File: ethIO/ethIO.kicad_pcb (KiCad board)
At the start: 4 copper layers, 30 x 50 mm, 62 parts, among them IC3 TLV61225DC, J6 MISC, J7 HR911130A1, U10 RTL8211E-VB-CG, Y1 25MHz

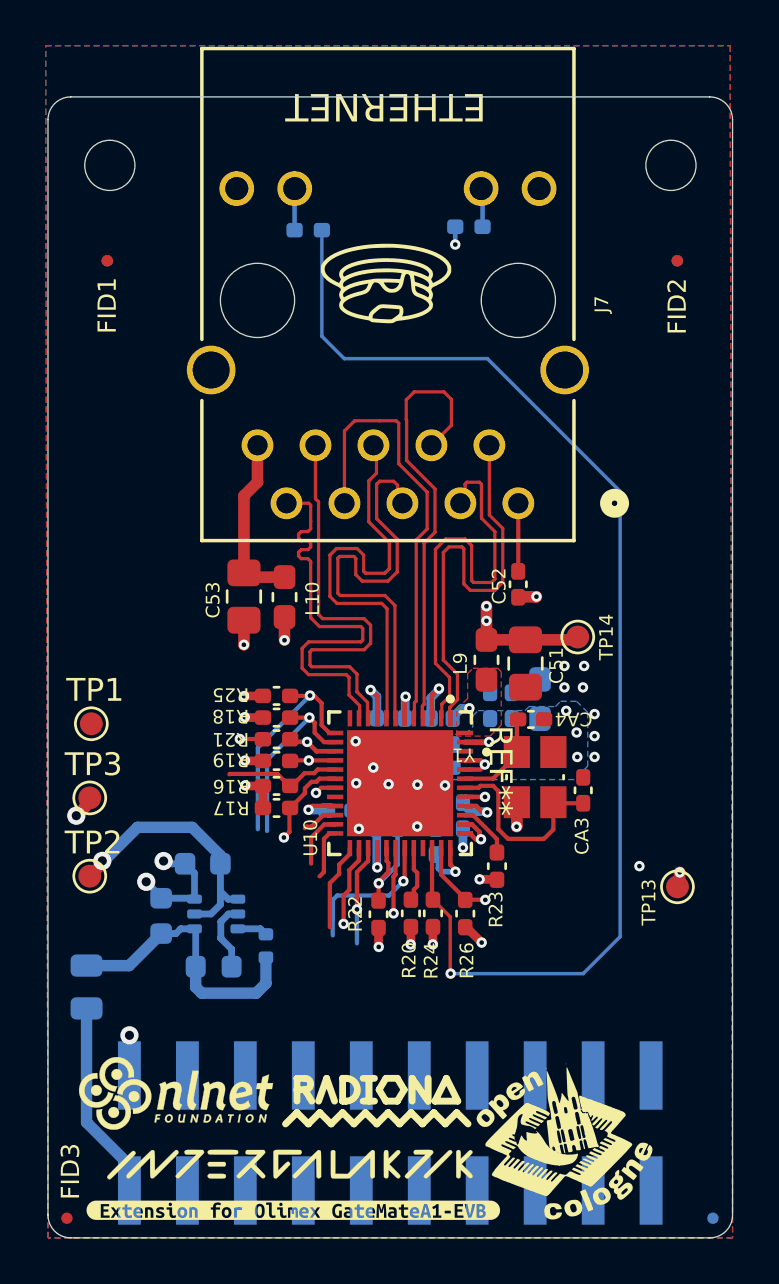
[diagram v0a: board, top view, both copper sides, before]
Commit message: Updating ethIO
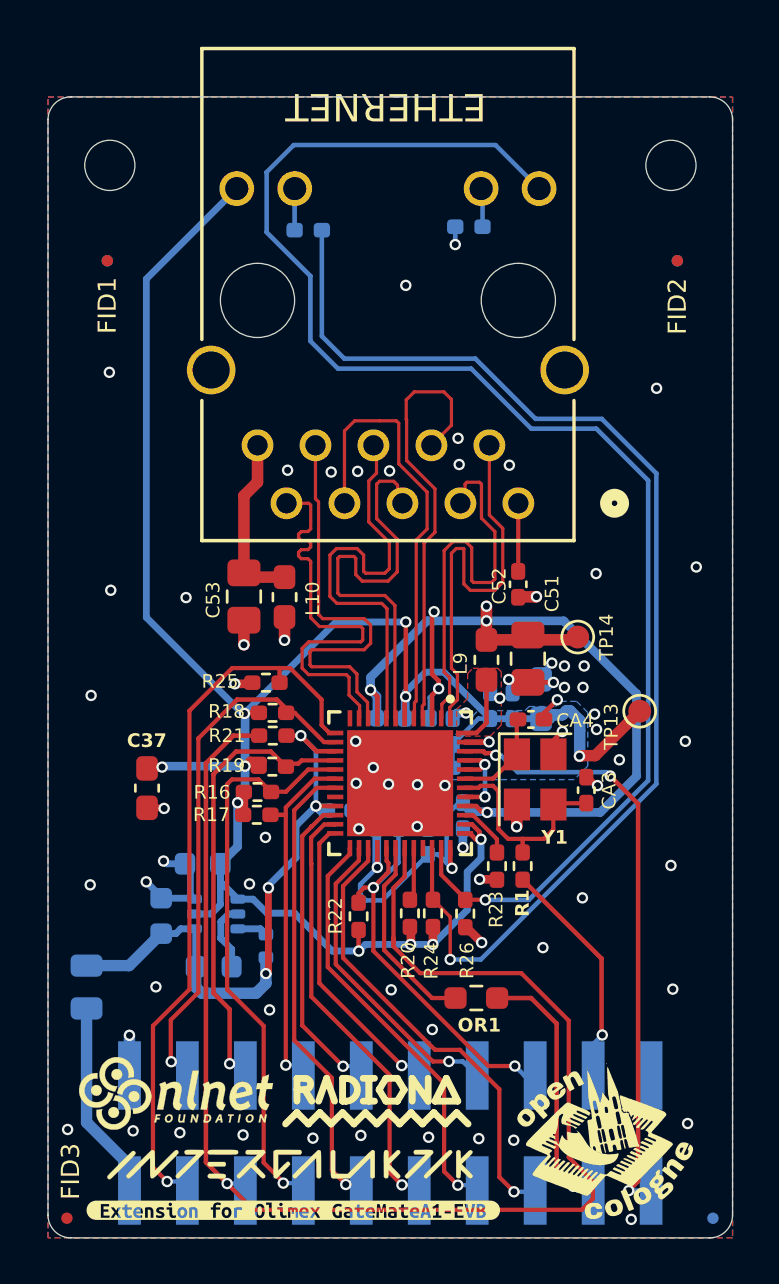
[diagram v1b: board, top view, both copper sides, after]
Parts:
- removed G***: LOGO, memes:pancakes
- removed TP1: 3V3, TestPoint:TestPoint_Pad_D1.0mm
- removed TP2: 2V5, TestPoint:TestPoint_Pad_D1.0mm
- removed TP3: GND, TestPoint:TestPoint_Pad_D1.0mm
- added C37: 4.7uF, Capacitor_SMD:C_0603_1608Metric_Pad1.08x0.95mm_HandSolder, F.Cu at (89.6, 62.1)
- added OR1: 0R, Resistor_SMD:R_0603_1608Metric_Pad0.98x0.95mm_HandSolder, F.Cu at (104.0, 71.3)
- added R1: 0R, Resistor_SMD:R_0402_1005Metric_Pad0.72x0.64mm_HandSolder, F.Cu at (106.0, 65.5)
- J7: footprint Libraries:HR911130A_HAN -> HR911130A1:HR911130A_HAN
- U10: footprint Libraries:RTL8211E-VB-CG -> RTL8211E-VB-CG:RTL8211E-VB-CG
- Y1: footprint Libraries:XTAL_TSX-3225_25.0000MF10P-C0 -> Crystal:Crystal_SMD_SeikoEpson_TSX3225-4Pin_3.2x2.5mm
- moved TP13 7.87 mm to (111.2, 58.8)
- moved H3 1.78 mm to (109.5, 77.6)
- moved R17 0.92 mm to (94.4, 63.3)
- moved R22 0.88 mm to (98.9, 67.7)
- moved R16 0.88 mm to (94.4, 62.3)
- moved R25 0.74 mm to (94.8, 57.5)
- moved C49 0.34 mm to (101.9, 64.5)
- moved R19 0.31 mm to (95.1, 61.2)
- moved R18 0.27 mm to (95.1, 58.8)
- moved C51 0.23 mm to (106.3, 56.5)
- moved R21 0.23 mm to (95.1, 59.8)
- moved CA3 0.14 mm to (108.8, 62.2)
- moved Y1 0.10 mm to (106.6, 61.7), turned to -90 degrees
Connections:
- net +36V renamed VDD10_EPHY
- net /Main Sheet/NB_B8 renamed /Main Sheet/NB_B8_8N
- net /Sheet2/LED0_AD0 renamed /Main Sheet/Ethernet/LED0_AD0
- net /Sheet2/LED1_AD1 renamed /Main Sheet/Ethernet/LED1_AD1
- net /Sheet2/LED2_RXDLY renamed /Main Sheet/Ethernet/LED2_RXDLY
- net /Sheet2/MDI0_N renamed /Main Sheet/Ethernet/MDI0_N
- net /Sheet2/MDI0_P renamed /Main Sheet/Ethernet/MDI0_P
- net /Sheet2/MDI1_N renamed /Main Sheet/Ethernet/MDI1_N
- net /Sheet2/MDI1_P renamed /Main Sheet/Ethernet/MDI1_P
- net /Sheet2/MDI2_N renamed /Main Sheet/Ethernet/MDI2_N
- net /Sheet2/MDI2_P renamed /Main Sheet/Ethernet/MDI2_P
- net /Sheet2/MDI3_N renamed /Main Sheet/Ethernet/MDI3_N
- net /Sheet2/MDI3_P renamed /Main Sheet/Ethernet/MDI3_P
- net /Sheet2/REGOUT renamed /Main Sheet/Ethernet/REGOUT
- net /Sheet2/RGMII_GR- renamed /Main Sheet/Ethernet/RGMII_GR-
- net /Sheet2/RGMI_YE- renamed /Main Sheet/Ethernet/RGMI_YE-
- net /Sheet2/XTAL_IN renamed /Main Sheet/Ethernet/XTAL_IN
- net /Sheet2/XTAL_OUT renamed /Main Sheet/Ethernet/XTAL_OUT
- C13 pad 1: +2V5 -> +VCC_LOW
- C14 pad 1: +3V3 -> +VCC_HIGH
- C38 pad 1: VCC -> +VCC_HIGH
- C39 pad 1: PHY_RST -> /Main Sheet/NB_B6_6N
- C41 pad 1: VCC -> +VCC_HIGH
- C43 pad 1: VCC -> +VCC_HIGH
- C45 pad 1: VCC -> +VCC_HIGH
- C47 pad 1: VCC -> +VCC_HIGH
- C48 pad 1: +1V8 -> +VCC_LOW
- C50 pad 1: VCC -> +VCC_HIGH
- F1 pad 2: +2V5 -> +VCC_LOW
- IC3 pad 1: +2V5 -> +VCC_LOW
- IC3 pad 2: +3V3 -> +VCC_HIGH
- IC3 pad 4: +3V3 -> +VCC_HIGH
- J6 pad 10: /Main Sheet/NB_B3 -> /Main Sheet/NB_B3_3N
- J6 pad 11: /Main Sheet/NB_A4 -> /Main Sheet/NB_A4_4P
- J6 pad 12: /Main Sheet/NB_B4 -> /Main Sheet/NB_B4_4N
- J6 pad 13: /Main Sheet/NB_A5 -> /Main Sheet/NB_A5_5P
- J6 pad 14: /Main Sheet/NB_B5 -> /Main Sheet/NB_B5_5N
- J6 pad 15: /Main Sheet/NB_A6 -> /Main Sheet/NB_A6_6P
- J6 pad 16: /Main Sheet/NB_B6 -> /Main Sheet/NB_B6_6N
- J6 pad 17: /Main Sheet/NB_A7 -> /Main Sheet/NB_A7_7P
- J6 pad 18: /Main Sheet/NB_B7 -> /Main Sheet/NB_B7_7N
- J6 pad 19: /Main Sheet/NB_A8 -> /Main Sheet/NB_A8_8P
- J6 pad 3: /Main Sheet/NB_A0 -> /Main Sheet/NB_A0_0P
- J6 pad 4: /Main Sheet/NB_B0 -> /Main Sheet/NB_B0_0N
- J6 pad 5: /Main Sheet/NB_A1 -> /Main Sheet/NB_A1_1P
- J6 pad 6: /Main Sheet/NB_B1 -> /Main Sheet/NB_B1_1N
- J6 pad 7: /Main Sheet/NB_A2 -> /Main Sheet/NB_A2_2P
- J6 pad 8: /Main Sheet/NB_B2 -> /Main Sheet/NB_B2_2N
- J6 pad 9: /Main Sheet/NB_A3 -> /Main Sheet/NB_A3_3P
- J7 pad 14: VCC -> +VCC_HIGH
- L1 pad 2: +2V5 -> +VCC_LOW
- R15 pad 1: +2V5 -> +VCC_LOW
- R16 pad 1: VCC -> +VCC_HIGH
- R16 pad 2: PHY_RXD2 -> /Main Sheet/NB_A2_2P
- R17 pad 1: VCC -> +VCC_HIGH
- R17 pad 2: PHY_RXD3 -> /Main Sheet/NB_B2_2N
- R18 pad 1: VCC -> +VCC_HIGH
- R18 pad 2: PHY_RXD0 -> /Main Sheet/NB_B0_0N
- R19 pad 1: VCC -> +VCC_HIGH
- R19 pad 2: PHY_RXD1 -> /Main Sheet/NB_B1_1N
- R20 pad 1: VCC -> +VCC_HIGH
- R21 pad 1: +1V8 -> +VCC_LOW
- R21 pad 2: MAC_MDIO -> /Main Sheet/NB_A1_1P
- R22 pad 1: PHY_RST -> /Main Sheet/NB_B6_6N
- R22 pad 2: VCC -> +VCC_HIGH
- R24 pad 1: VCC -> +VCC_HIGH
- R25 pad 2: ETH_RXCTL -> /Main Sheet/NB_A0_0P
- TP13 pad 1: VCC -> +VCC_HIGH
- U10 pad 13: ETH_RXCTL -> /Main Sheet/NB_A0_0P
- U10 pad 14: PHY_RXD0 -> /Main Sheet/NB_B0_0N
- U10 pad 15: +1V8 -> +VCC_LOW
- U10 pad 16: PHY_RXD1 -> /Main Sheet/NB_B1_1N
- U10 pad 17: PHY_RXD2 -> /Main Sheet/NB_A2_2P
- U10 pad 18: PHY_RXD3 -> /Main Sheet/NB_B2_2N
- U10 pad 19: PHY_RXCLK -> /Main Sheet/NB_A3_3P
- U10 pad 21: +1V8 -> +VCC_LOW
- U10 pad 22: PHY_TXCLK -> /Main Sheet/NB_B3_3N
- U10 pad 23: PHY_TXD0 -> /Main Sheet/NB_A4_4P
- U10 pad 24: PHY_TXD1 -> /Main Sheet/NB_B4_4N
- U10 pad 25: PHY_TXD2 -> /Main Sheet/NB_A5_5P
- U10 pad 26: PHY_TXD3 -> /Main Sheet/NB_B5_5N
- U10 pad 27: PHY_TXEN -> /Main Sheet/NB_A6_6P
- U10 pad 29: PHY_RST -> /Main Sheet/NB_B6_6N
- U10 pad 30: /Sheet2/MAC_MDC -> /Main Sheet/Ethernet/MAC_MDC
- U10 pad 31: MAC_MDIO -> /Main Sheet/NB_A1_1P
- U10 pad 37: VCC -> +VCC_HIGH
- U10 pad 38: VCC -> +VCC_HIGH
- U10 pad 41: VCC -> +VCC_HIGH
- U10 pad 44: VCC -> +VCC_HIGH
- U10 pad 45: VCC -> +VCC_HIGH
- U10 pad 46: unconnected-(U10-CLK125-Pad46) -> /Main Sheet/NB_A8_8P
- U10 pad 6: VCC -> +VCC_HIGH
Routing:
- net +VCC_HIGH: track 0.00 -> 100.8 mm, vias 0 -> 13
- net /Main Sheet/NB_A1_1P: track 0.00 -> 61.3 mm, vias 0 -> 1
- net /Main Sheet/Ethernet/LED1_AD1: track 3.56 -> 64.8 mm
- net VDD10_EPHY: track 18.7 -> 57.1 mm, vias 7 -> 8
- net /Main Sheet/NB_A0_0P: track 0.00 -> 32.2 mm, vias 0 -> 1
- net +VCC_LOW: track 0.00 -> 27.9 mm, vias 0 -> 4
- net /Main Sheet/NB_A8_8P: track 0.00 -> 26.6 mm, vias 0 -> 3
- net /Main Sheet/NB_A2_2P: track 0.00 -> 25.0 mm, vias 0 -> 1
- net /Main Sheet/NB_B0_0N: track 0.00 -> 23.5 mm, vias 0 -> 1
- net /Main Sheet/NB_A3_3P: track 0.00 -> 20.4 mm, vias 0 -> 1
- net /Main Sheet/NB_A6_6P: track 0.00 -> 20.2 mm, vias 0 -> 1
- net /Main Sheet/NB_B1_1N: track 0.00 -> 19.8 mm, vias 0 -> 1
- net /Main Sheet/NB_A4_4P: track 0.00 -> 19.0 mm, vias 0 -> 1
- net /Main Sheet/NB_A5_5P: track 0.00 -> 18.5 mm, vias 0 -> 1
- net /Main Sheet/NB_B6_6N: track 0.00 -> 18.4 mm, vias 0 -> 2
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- added copper zone on F.Cu, net (none)
- added copper zone on B.Cu, net +VCC_HIGH
- removed copper zone on F.Cu, net /Main Sheet/Ethernet/REGOUT
- removed copper zone on B.Cu, net VCC
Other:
- rule pad_to_mask_clearance: 0.1 -> 0.05
